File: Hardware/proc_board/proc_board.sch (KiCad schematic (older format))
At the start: 12 parts, among them J1 Conn_01x40, U1 74HC21, U2 W65C02SxP, U3 HM62256BLP, U4 28C256, U5 74HC00

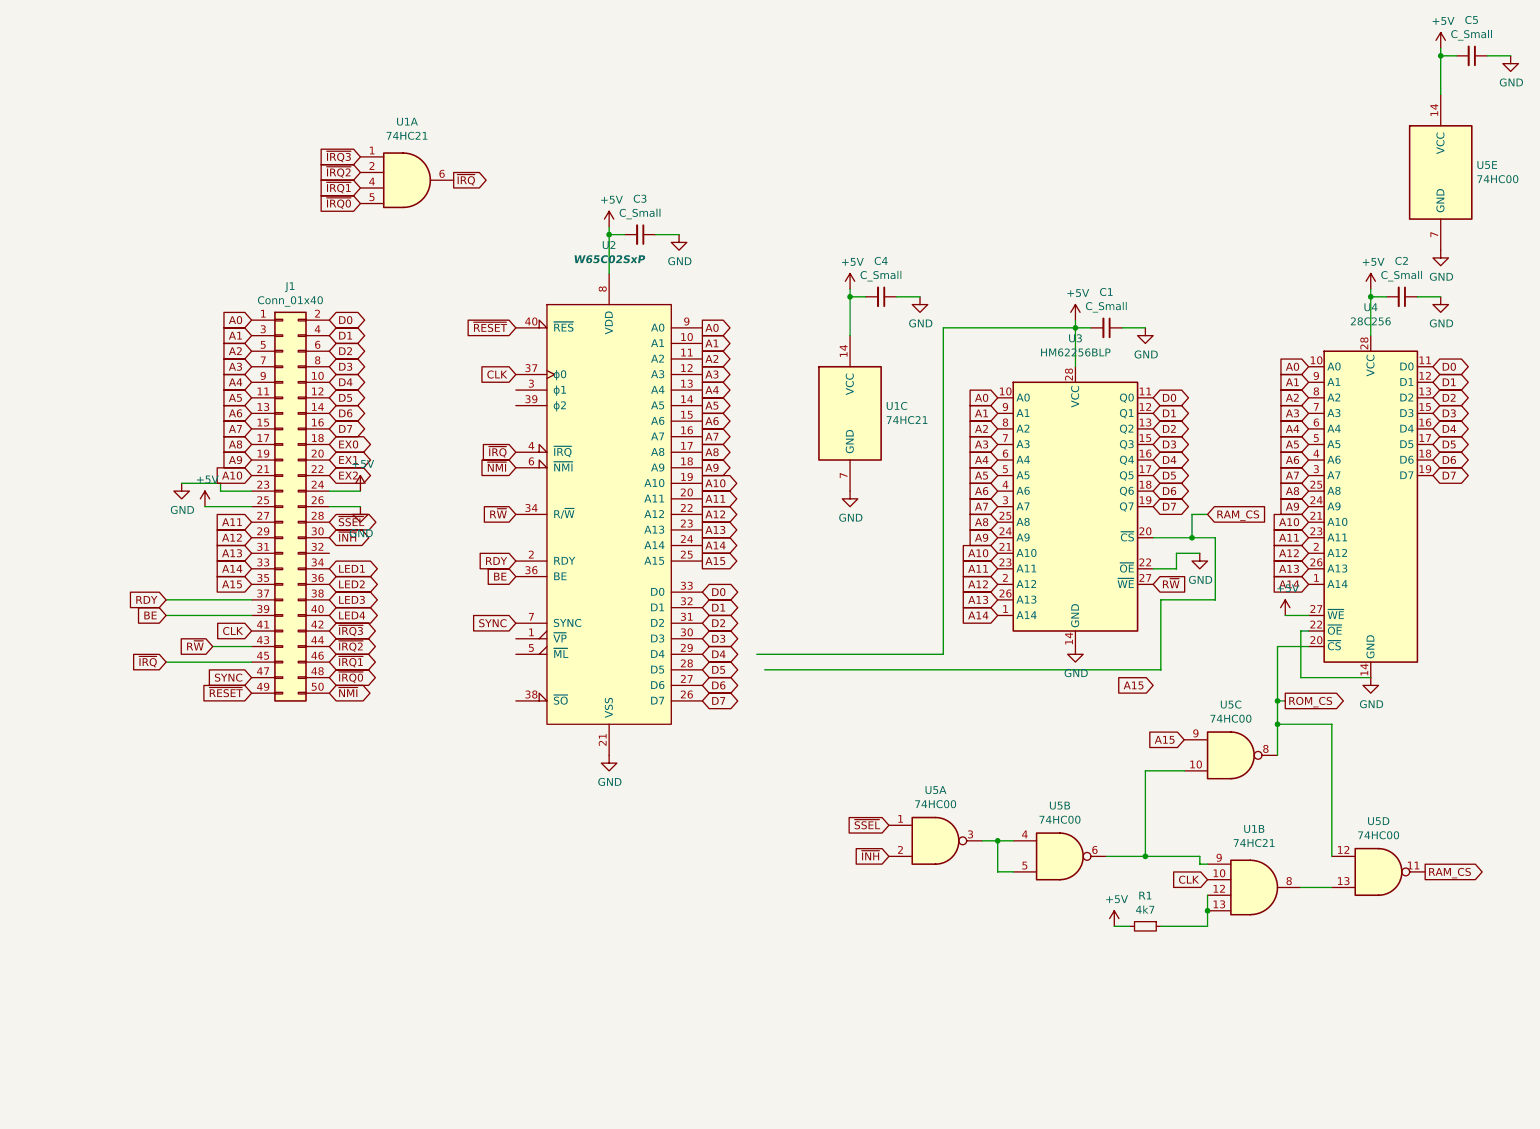
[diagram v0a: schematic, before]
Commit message: Clean up schematics and add pdfs
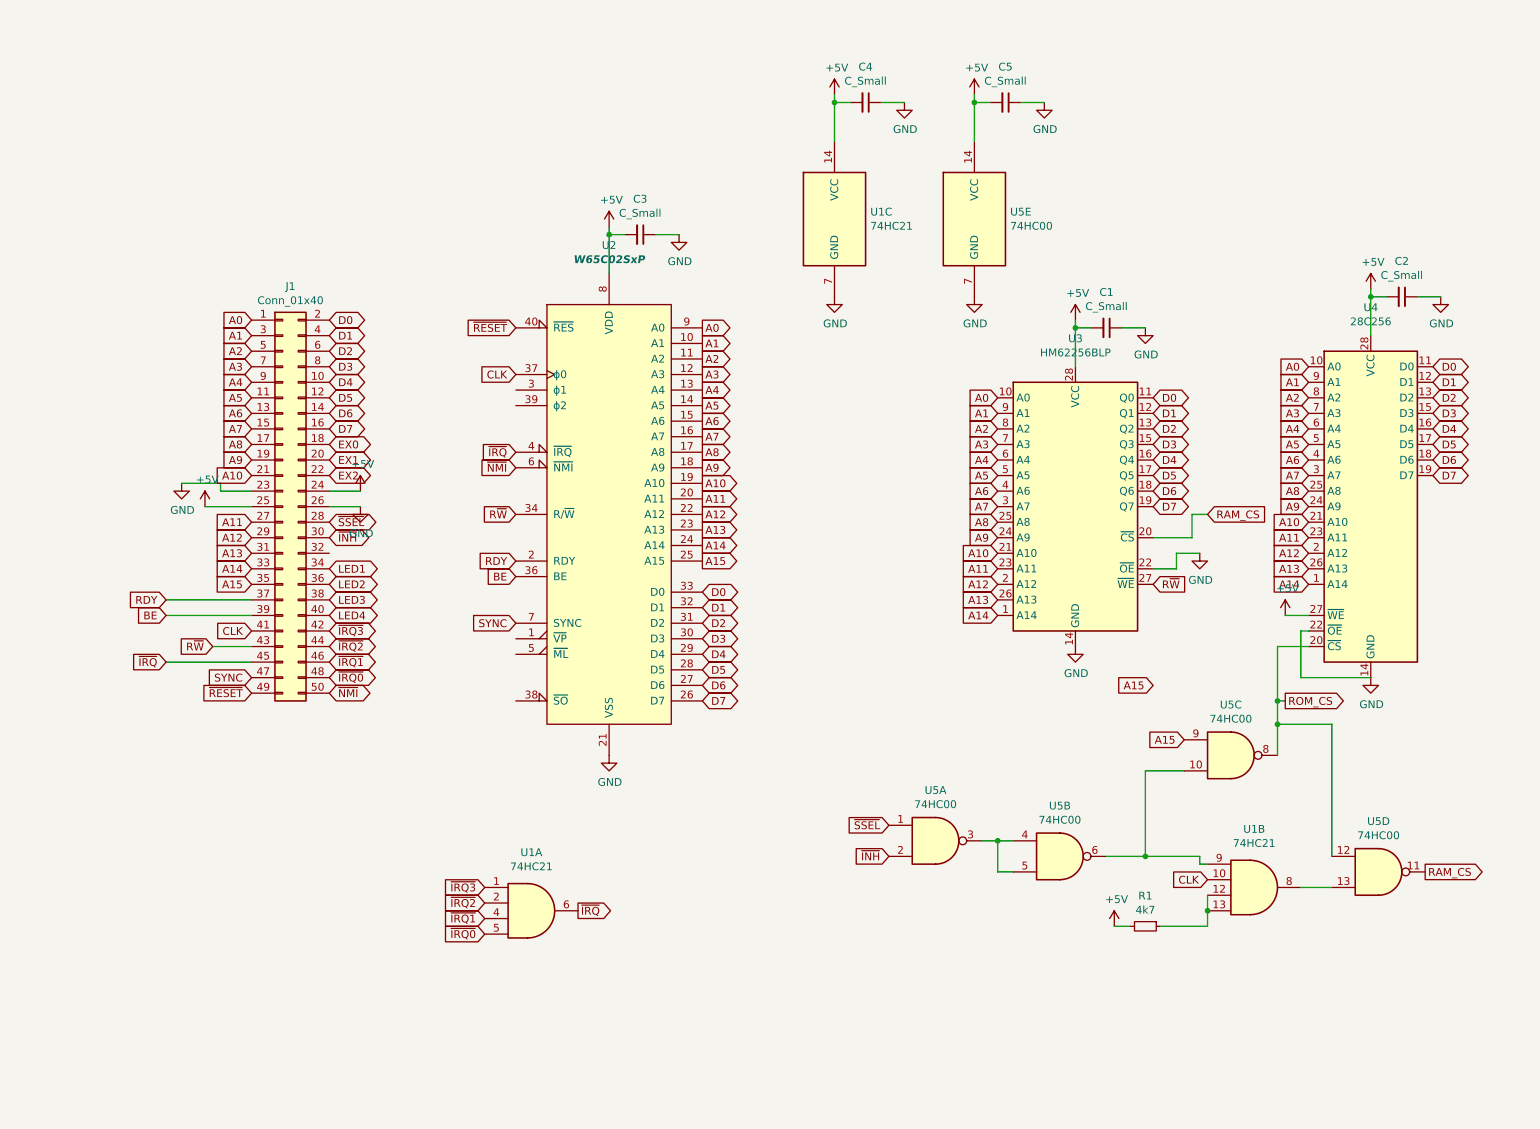
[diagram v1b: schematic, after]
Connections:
- wire segments 70 -> 62
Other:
- moved on the sheet: C4, C5, U1A, U1C, U5E
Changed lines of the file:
@@
 L 74xx:74LS21 U1
 U 1 1 5FD70EEB
-P 3300 1350
-F 0 "U1" H 3300 1725 50  0000 C CNN
-F 1 "74HC21" H 3300 1634 50  0000 C CNN
-F 2 "Package_DIP:DIP-14_W7.62mm_Socket" H 3300 1350 50  0001 C CNN
-F 3 "http://www.ti.com/lit/gpn/sn74LS21" H 3300 1350 50  0001 C CNN
-	1    3300 1350
+P 4100 6050
+F 0 "U1" H 4100 6425 50  0000 C CNN
+F 1 "74HC21" H 4100 6334 50  0000 C CNN
+F 2 "Package_DIP:DIP-14_W7.62mm_Socket" H 4100 6050 50  0001 C CNN
+F 3 "http://www.ti.com/lit/gpn/sn74LS21" H 4100 6050 50  0001 C CNN
+	1    4100 6050
 	1    0    0    -1
 $EndComp
@@
 L 74xx:74LS21 U1
 U 3 1 5FD74C69
-P 6150 2850
-F 0 "U1" H 6380 2896 50  0000 L CNN
-F 1 "74HC21" H 6380 2805 50  0000 L CNN
-F 2 "Package_DIP:DIP-14_W7.62mm_Socket" H 6150 2850 50  0001 C CNN
-F 3 "http://www.ti.com/lit/gpn/sn74LS21" H 6150 2850 50  0001 C CNN
-	3    6150 2850
+P 6050 1600
+F 0 "U1" H 6280 1646 50  0000 L CNN
+F 1 "74HC21" H 6280 1555 50  0000 L CNN
+F 2 "Package_DIP:DIP-14_W7.62mm_Socket" H 6050 1600 50  0001 C CNN
+F 3 "http://www.ti.com/lit/gpn/sn74LS21" H 6050 1600 50  0001 C CNN
+	3    6050 1600
 	1    0    0    -1
 $EndComp
@@
 L power:+5V #PWR0108
 U 1 1 5FD775B0
-P 6150 2050
-F 0 "#PWR0108" H 6150 1900 50  0001 C CNN
-F 1 "+5V" H 6165 2223 50  0000 C CNN
-F 2 "" H 6150 2050 50  0001 C CNN
-F 3 "" H 6150 2050 50  0001 C CNN
-	1    6150 2050
-	1    0    0    -1
-$EndComp
-Wire Wire Line
-	6150 2350 6150 2100
+P 6050 800
+F 0 "#PWR0108" H 6050 650 50  0001 C CNN
+F 1 "+5V" H 6065 973 50  0000 C CNN
+F 2 "" H 6050 800 50  0001 C CNN
+F 3 "" H 6050 800 50  0001 C CNN
+	1    6050 800
+	1    0    0    -1
+$EndComp
+Wire Wire Line
+	6050 1100 6050 850
 $Comp
 L Device:C_Small C4
 U 1 1 5FD775B7
-P 6350 2100
-F 0 "C4" V 6121 2100 50  0000 C CNN
-F 1 "C_Small" V 6212 2100 50  0000 C CNN
-F 2 "Capacitor_SMD:C_1206_3216Metric_Pad1.42x1.75mm_HandSolder" H 6350 2100 50  0001 C CNN
-F 3 "~" H 6350 2100 50  0001 C CNN
-	1    6350 2100
+P 6250 850
+F 0 "C4" V 6021 850 50  0000 C CNN
+F 1 "C_Small" V 6112 850 50  0000 C CNN
+F 2 "Capacitor_SMD:C_1206_3216Metric_Pad1.42x1.75mm_HandSolder" H 6250 850 50  0001 C CNN
+F 3 "~" H 6250 850 50  0001 C CNN
+	1    6250 850
 	0    1    1    0
 $EndComp
@@
 L power:GND #PWR0109
 U 1 1 5FD775BD
-P 6600 2100
-F 0 "#PWR0109" H 6600 1850 50  0001 C CNN
-F 1 "GND" H 6605 1927 50  0000 C CNN
-F 2 "" H 6600 2100 50  0001 C CNN
-F 3 "" H 6600 2100 50  0001 C CNN
-	1    6600 2100
-	1    0    0    -1
-$EndComp
-Wire Wire Line
-	6600 2100 6450 2100
-Wire Wire Line
-	6250 2100 6150 2100
-Connection ~ 6150 2100
-Wire Wire Line
-	6150 2100 6150 2050
+P 6500 850
+F 0 "#PWR0109" H 6500 600 50  0001 C CNN
+F 1 "GND" H 6505 677 50  0000 C CNN
+F 2 "" H 6500 850 50  0001 C CNN
+F 3 "" H 6500 850 50  0001 C CNN
+	1    6500 850
+	1    0    0    -1
+$EndComp
+Wire Wire Line
+	6500 850  6350 850
+Wire Wire Line
+	6150 850  6050 850
+Connection ~ 6050 850
+Wire Wire Line
+	6050 850  6050 800
 $Comp
 L power:GND #PWR0110
 U 1 1 5FD782E3
-P 6150 3350
-F 0 "#PWR0110" H 6150 3100 50  0001 C CNN
-F 1 "GND" H 6155 3177 50  0000 C CNN
-F 2 "" H 6150 3350 50  0001 C CNN
-F 3 "" H 6150 3350 50  0001 C CNN
-	1    6150 3350
-	1    0    0    -1
-$EndComp
-Text GLabel 3000 1500 0    50   Input ~ 0
+P 6050 2100
+F 0 "#PWR0110" H 6050 1850 50  0001 C CNN
+F 1 "GND" H 6055 1927 50  0000 C CNN
+F 2 "" H 6050 2100 50  0001 C CNN
+F 3 "" H 6050 2100 50  0001 C CNN
+	1    6050 2100
+	1    0    0    -1
+$EndComp
+Text GLabel 3800 6200 0    50   Input ~ 0
 ~IRQ0~
-Text GLabel 3000 1400 0    50   Input ~ 0
+Text GLabel 3800 6100 0    50   Input ~ 0
 ~IRQ1~
-Text GLabel 3000 1300 0    50   Input ~ 0
+Text GLabel 3800 6000 0    50   Input ~ 0
 ~IRQ2~
-Text GLabel 3000 1200 0    50   Input ~ 0
+Text GLabel 3800 5900 0    50   Input ~ 0
 ~IRQ3~
-Text GLabel 3600 1350 2    50   Output ~ 0
+Text GLabel 4400 6050 2    50   Output ~ 0
 ~IRQ~
 Wire Wire Line
 	8450 6050 8450 6150
-$Comp
-L Memory_RAM:HM62256BLP U3
-U 1 1 5FDE3197
-P 7600 3450
-F 0 "U3" H 7600 4531 50  0000 C CNN
-F 1 "HM62256BLP" H 7600 4440 50  0000 C CNN
-F 2 "Package_DIP:DIP-28_W7.62mm_Socket" H 7600 3350 50  0001 C CNN
-F 3 "https://web.mit.edu/6.115/www/document/62256.pdf" H 7600 3350 50  0001 C CNN
-	1    7600 3450
-	1    0    0    -1
-$EndComp
 $Comp
 L Memory_EEPROM:28C256 U4
@@
 L 74xx:74HC00 U5
 U 5 1 5FDF7440
-P 9950 1300
-F 0 "U5" H 10180 1346 50  0000 L CNN
-F 1 "74HC00" H 10180 1255 50  0000 L CNN
-F 2 "Package_DIP:DIP-14_W7.62mm_Socket" H 9950 1300 50  0001 C CNN
-F 3 "http://www.ti.com/lit/gpn/sn74hc00" H 9950 1300 50  0001 C CNN
-	5    9950 1300
+P 6950 1600
+F 0 "U5" H 7180 1646 50  0000 L CNN
+F 1 "74HC00" H 7180 1555 50  0000 L CNN
+F 2 "Package_DIP:DIP-14_W7.62mm_Socket" H 6950 1600 50  0001 C CNN
+F 3 "http://www.ti.com/lit/gpn/sn74hc00" H 6950 1600 50  0001 C CNN
+	5    6950 1600
 	1    0    0    -1
 $EndComp
@@
 L power:+5V #PWR0114
 U 1 1 5FE29AEB
-P 9950 500
-F 0 "#PWR0114" H 9950 350 50  0001 C CNN
-F 1 "+5V" H 9965 673 50  0000 C CNN
-F 2 "" H 9950 500 50  0001 C CNN
-F 3 "" H 9950 500 50  0001 C CNN
-	1    9950 500
-	1    0    0    -1
-$EndComp
-Wire Wire Line
-	9950 800  9950 550
+P 6950 800
+F 0 "#PWR0114" H 6950 650 50  0001 C CNN
+F 1 "+5V" H 6965 973 50  0000 C CNN
+F 2 "" H 6950 800 50  0001 C CNN
+F 3 "" H 6950 800 50  0001 C CNN
+	1    6950 800
+	1    0    0    -1
+$EndComp
+Wire Wire Line
+	6950 1100 6950 850
 $Comp
 L Device:C_Small C5
 U 1 1 5FE29AF2
-P 10150 550
-F 0 "C5" V 9921 550 50  0000 C CNN
-F 1 "C_Small" V 10012 550 50  0000 C CNN
-F 2 "Capacitor_SMD:C_1206_3216Metric_Pad1.42x1.75mm_HandSolder" H 10150 550 50  0001 C CNN
-F 3 "~" H 10150 550 50  0001 C CNN
-	1    10150 550
+P 7150 850
+F 0 "C5" V 6921 850 50  0000 C CNN
+F 1 "C_Small" V 7012 850 50  0000 C CNN
+F 2 "Capacitor_SMD:C_1206_3216Metric_Pad1.42x1.75mm_HandSolder" H 7150 850 50  0001 C CNN
+F 3 "~" H 7150 850 50  0001 C CNN
+	1    7150 850
 	0    1    1    0
 $EndComp
@@
 L power:GND #PWR0115
 U 1 1 5FE29AF8
-P 10400 550
-F 0 "#PWR0115" H 10400 300 50  0001 C CNN
-F 1 "GND" H 10405 377 50  0000 C CNN
-F 2 "" H 10400 550 50  0001 C CNN
-F 3 "" H 10400 550 50  0001 C CNN
-	1    10400 550
-	1    0    0    -1
-$EndComp
-Wire Wire Line
-	10400 550  10250 550
-Wire Wire Line
-	10050 550  9950 550
-Connection ~ 9950 550
-Wire Wire Line
-	9950 550  9950 500
+P 7400 850
+F 0 "#PWR0115" H 7400 600 50  0001 C CNN
+F 1 "GND" H 7405 677 50  0000 C CNN
+F 2 "" H 7400 850 50  0001 C CNN
+F 3 "" H 7400 850 50  0001 C CNN
+	1    7400 850
+	1    0    0    -1
+$EndComp
+Wire Wire Line
+	7400 850  7250 850
+Wire Wire Line
+	7050 850  6950 850
+Connection ~ 6950 850
+Wire Wire Line
+	6950 850  6950 800
 $Comp
 L power:GND #PWR0116
@@
 L power:GND #PWR0117
 U 1 1 5FE2AFAA
-P 9950 1800
-F 0 "#PWR0117" H 9950 1550 50  0001 C CNN
-F 1 "GND" H 9955 1627 50  0000 C CNN
-F 2 "" H 9950 1800 50  0001 C CNN
-F 3 "" H 9950 1800 50  0001 C CNN
-	1    9950 1800
+P 6950 2100
+F 0 "#PWR0117" H 6950 1850 50  0001 C CNN
+F 1 "GND" H 6955 1927 50  0000 C CNN
+F 2 "" H 6950 2100 50  0001 C CNN
+F 3 "" H 6950 2100 50  0001 C CNN
+	1    6950 2100
 	1    0    0    -1
 $EndComp
@@
 Wire Wire Line
 	8400 5750 8400 5700
-Wire Wire Line
-	7600 2300 6750 2300
-Wire Wire Line
-	6750 2300 6750 4400
-Wire Wire Line
-	6750 4400 5550 4400
-Wire Wire Line
-	8500 3650 8500 4050
-Wire Wire Line
-	8500 4050 8150 4050
-Wire Wire Line
-	8150 4050 8150 4500
-Wire Wire Line
-	8150 4500 5600 4500
-Wire Wire Line
-	8500 3650 8350 3650
 Connection ~ 8450 6050
 Wire Wire Line
@@
 Wire Wire Line
 	8350 3500 8350 3650
-Connection ~ 8350 3650
 Wire Wire Line
 	8350 3650 8100 3650
@@
 Wire Wire Line
 	8900 4700 8900 4850
+$Comp
+L Memory_RAM:HM62256BLP U3
+U 1 1 5FDE3197
+P 7600 3450
+F 0 "U3" H 7600 4531 50  0000 C CNN
+F 1 "HM62256BLP" H 7600 4440 50  0000 C CNN
+F 2 "Package_DIP:DIP-28_W7.62mm_Socket" H 7600 3350 50  0001 C CNN
+F 3 "https://web.mit.edu/6.115/www/document/62256.pdf" H 7600 3350 50  0001 C CNN
+	1    7600 3450
+	1    0    0    -1
+$EndComp
 $EndSCHEMATC

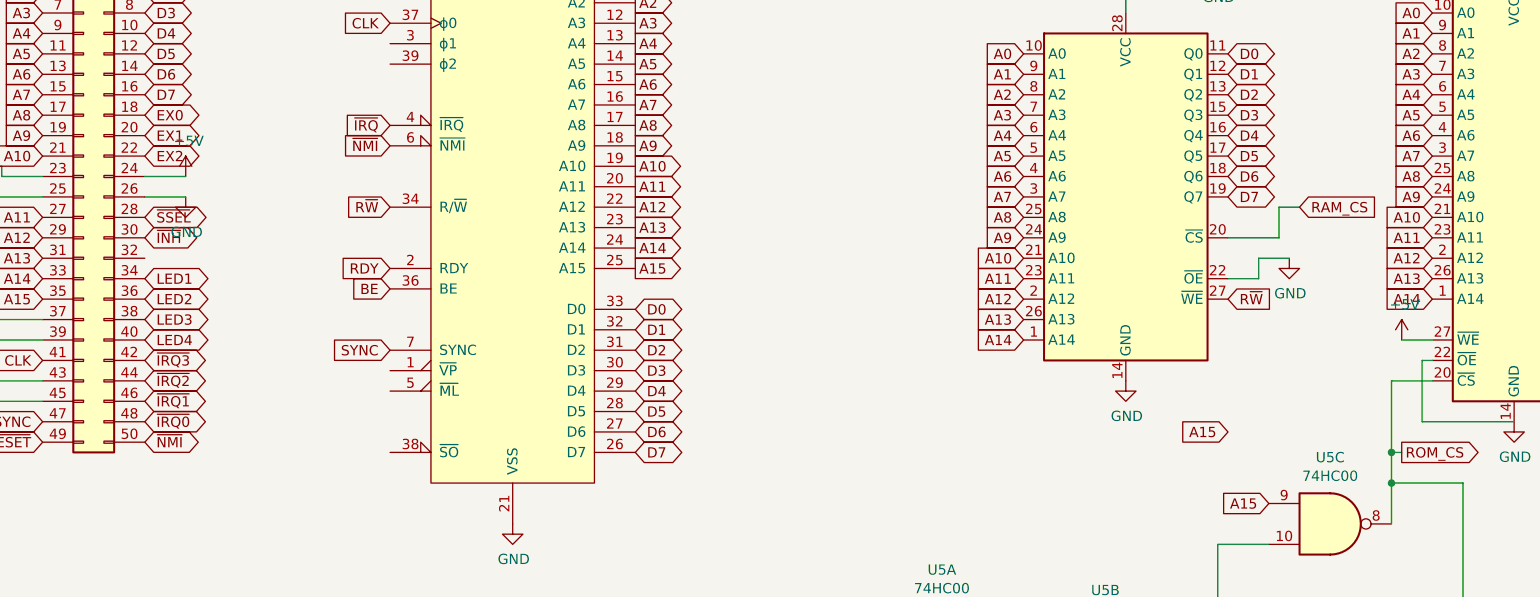
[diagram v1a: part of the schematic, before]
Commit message: Add clock stretching with counter and slow clock request from peripherals.
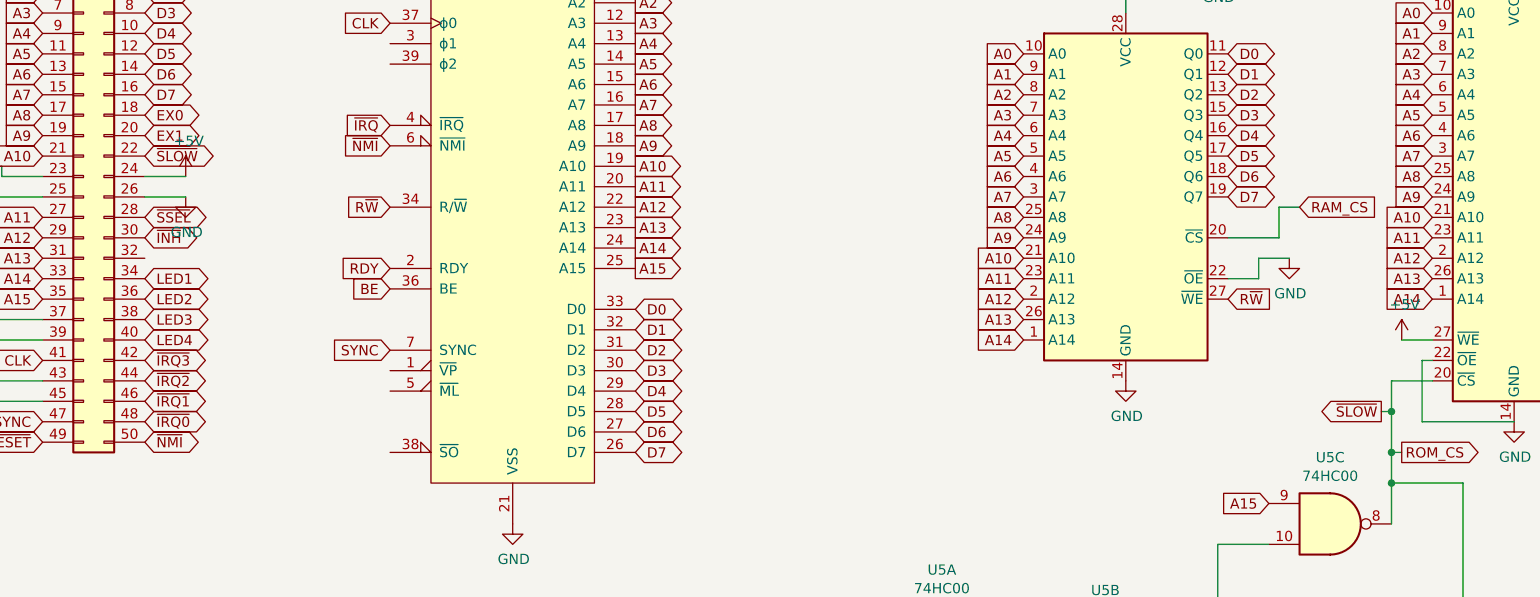
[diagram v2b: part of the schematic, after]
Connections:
- net EX2 is gone; now on net ROM_CS: J1.22 (Pin_22)
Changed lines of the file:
@@
 EX1
 Text GLabel 2800 3250 2    50   BiDi ~ 0
-EX2
+~SLOW~
 $Comp
 L 65xx:W65C02SxP U2
@@
 RAM_CS
 Wire Wire Line
-	8900 4350 8900 4700
+	8900 4350 8900 4500
 Wire Wire Line
 	8450 5750 8400 5750
@@
 	1    0    0    -1
 $EndComp
-Text GLabel 8100 4600 0    50   Input ~ 0
-A15
 Wire Wire Line
 	7200 5600 7100 5600
@@
 	1    0    0    -1
 $EndComp
+Text GLabel 8850 4500 0    50   Output ~ 0
+~SLOW~
+Wire Wire Line
+	8850 4500 8900 4500
+Connection ~ 8900 4500
+Wire Wire Line
+	8900 4500 8900 4700
 $EndSCHEMATC
